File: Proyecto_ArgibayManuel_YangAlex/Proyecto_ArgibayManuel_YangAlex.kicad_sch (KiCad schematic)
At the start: 35 parts, among them J1 Conn_01x02, J10 Con_1x2, J11 Con_1x2, J2 Conn_01x01, J3 Con_1x2, J4 Con_1x2, J5 Con_1x2, J6 Con_1x2, J7 Conn_01x03, J8 Conn_01x03, J9 Conn_01x03_Pin, SW1 SW_Push, SW2 SW_Push, SW3 SW_Push, SW4 SW_Push, U1 PIC18F258-I_SO, U2 HDC2010YPAR, U3 LT1716IS5TRMPBF, U4 LT1716IS5TRMPBF, U5 TXS0108EPW, Y1 Crystal

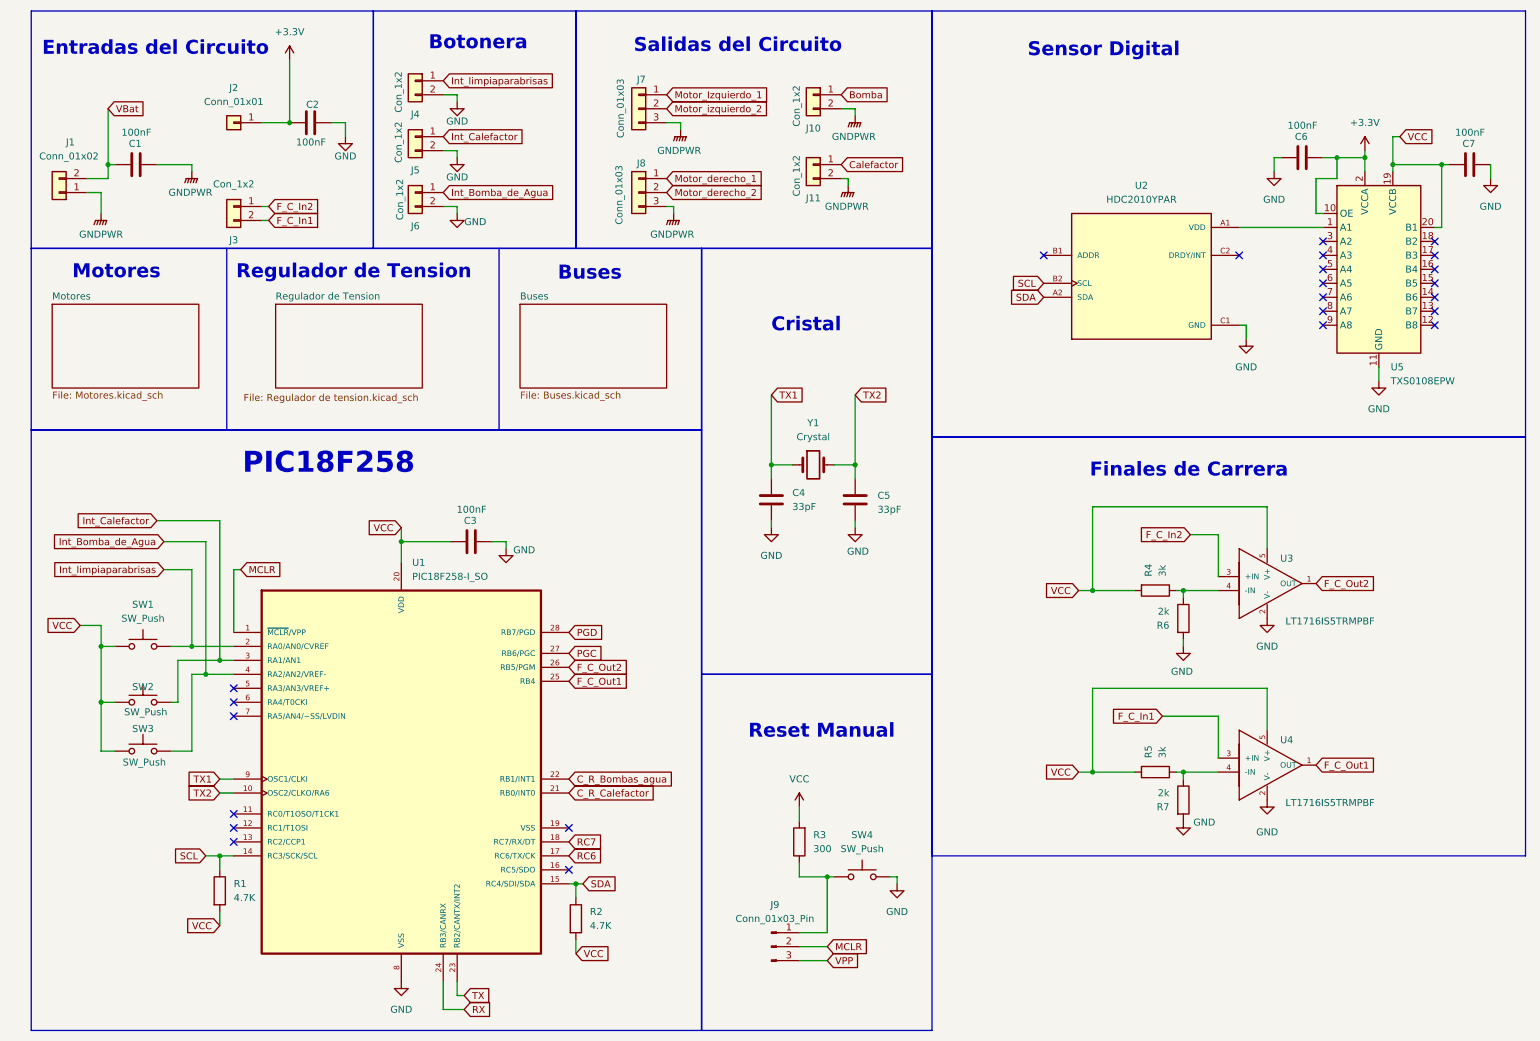
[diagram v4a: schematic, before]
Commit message: Cambio del sensor
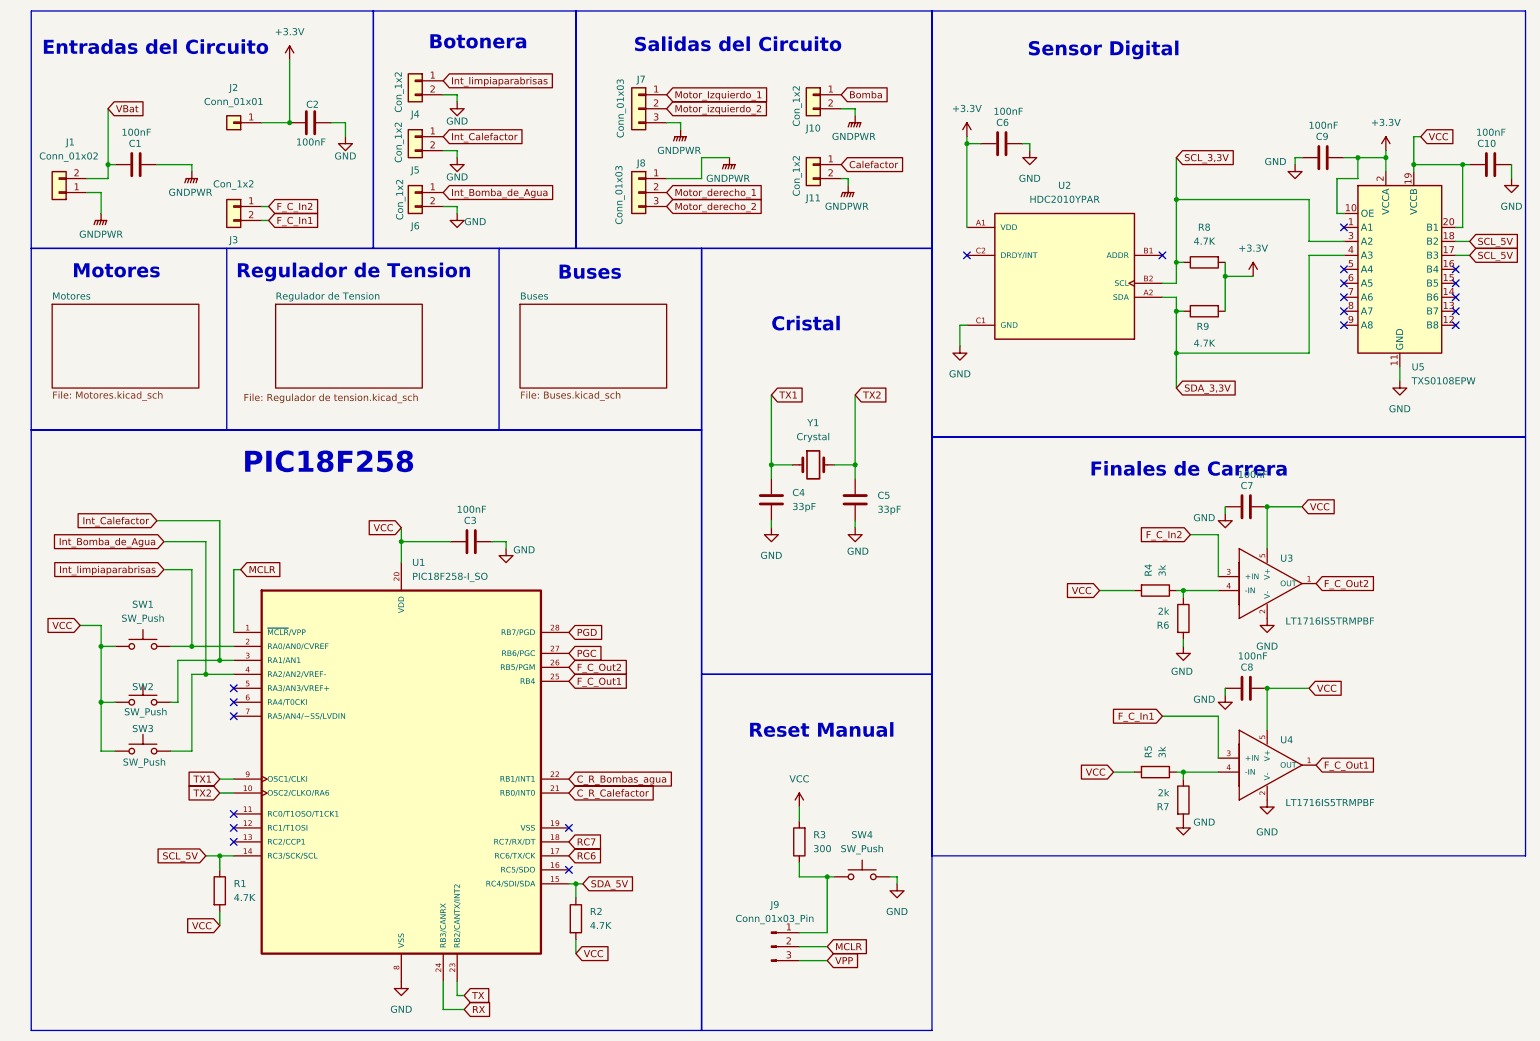
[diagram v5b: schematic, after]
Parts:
- added C6, C7, C8: 100nF, Capacitor_SMD:C_0805_2012Metric, symbol Device:C
- added R8, R9: 4.7K, Resistor_SMD:R_0805_2012Metric, symbol Device:R
- J10, J11: footprint Connector_PinHeader_2.54mm:PinHeader_1x02_P2.54mm_Vertical -> TerminalBlock_Phoenix:TerminalBlock_Phoenix_MKDS-3-2-5.08_1x02_P5.08mm_Horizontal
- J7, J8: footprint Connector_PinHeader_2.54mm:PinHeader_1x03_P2.54mm_Vertical -> TerminalBlock_Phoenix:TerminalBlock_Phoenix_MKDS-3-3-5.08_1x03_P5.08mm_Horizontal
- renumbered C7 to C10, C6 to C9
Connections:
- net +3.3V: now also U2.A1 (VDD), C6.2, R8.2, R9.2
- net GND: now also C6.1, C7.2, C8.2
- net GNDPWR: now also J8.1 (Pin_1); no longer J8.3 (Pin_3)
- net Motor_derecho_1: now also J8.2 (Pin_2); no longer J8.1 (Pin_1)
- net Motor_derecho_2: now also J8.3 (Pin_3); no longer J8.2 (Pin_2)
- net VCC: now also C7.1, C8.1
- net at U5.1 (A1): no longer U2.A1 (VDD)
- net SCL_5V: now reaches U5.17 (B3)
- net SCL_5V: now also R1.1, U1.14 (RC3/SCK/SCL), U5.18 (B2)
- net SCL_3,3V: now reaches U5.3 (A2)
- net SCL_3,3V: now also U2.B2 (SCL), R8.1
- net SDA_3,3V: now reaches U5.4 (A3)
- net SDA_3,3V: now also U2.A2 (SDA), R9.1
- removed net SCL: R1.1, U1.14 (RC3/SCK/SCL), U2.B2 (SCL)
- net SDA renamed SDA_5V
- net SDA_5V: no longer U2.A2 (SDA)
- no-connect marks 24 -> 21
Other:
- moved on the sheet: C10, C9, U2, U5

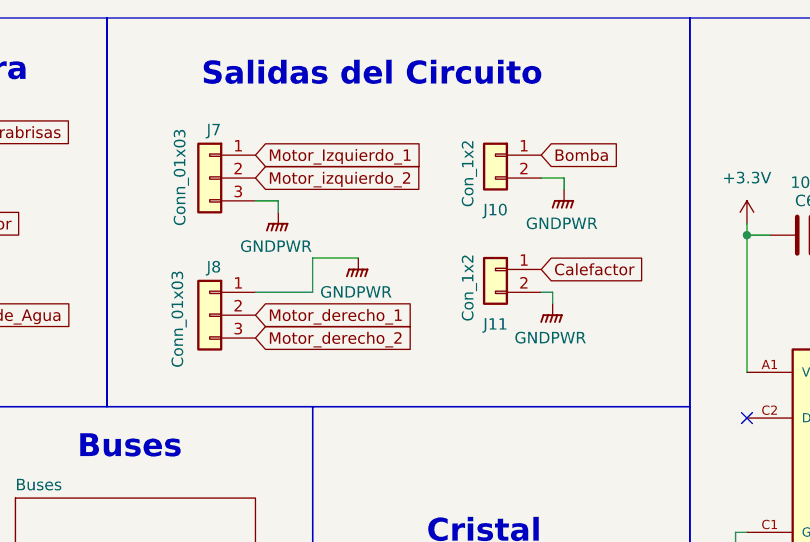
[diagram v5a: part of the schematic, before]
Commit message: Arreglo layout y esquematico (DRC correcto)
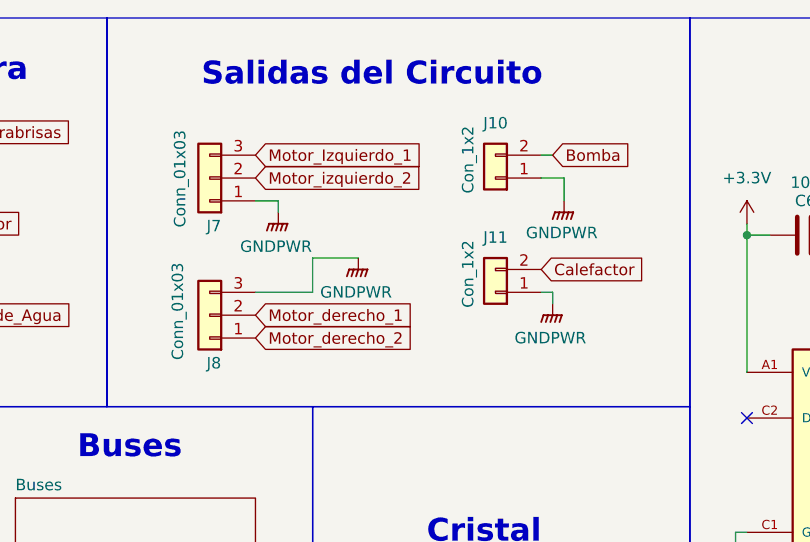
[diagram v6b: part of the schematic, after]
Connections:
- net Bomba: now also J10.2 (Pin_2); no longer J10.1 (Pin_1)
- net Calefactor: now also J11.2 (Pin_2); no longer J11.1 (Pin_1)
- net GNDPWR: now also J10.1 (Pin_1), J11.1 (Pin_1), J7.1 (Pin_1), J8.3 (Pin_3); no longer J10.2 (Pin_2), J11.2 (Pin_2), J7.3 (Pin_3), J8.1 (Pin_1)
- net Motor_Izquierdo_1: now also J7.3 (Pin_3); no longer J7.1 (Pin_1)
- net Motor_derecho_2: now also J8.1 (Pin_1); no longer J8.3 (Pin_3)
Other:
- moved on the sheet: J10, J11, J7, J8
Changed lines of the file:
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@@
 	(wire
 		(pts
+			(xy 162.56 30.48) (xy 162.56 33.02)
+		)
+		(stroke
+			(width 0)
+			(type default)
+		)
+	)
+	(wire
+		(pts
 			(xy 39.37 138.43) (xy 39.37 130.81)
 		)
@@
 	(wire
 		(pts
-			(xy 162.56 30.48) (xy 162.56 31.75)
-		)
-		(stroke
-			(width 0)
-			(type default)
-		)
-	)
-	(wire
-		(pts
 			(xy 147.32 95.25) (xy 151.13 95.25)
 		)
@@
 	(wire
 		(pts
-			(xy 245.11 74.93) (xy 245.11 57.15)
+			(xy 160.02 30.48) (xy 162.56 30.48)
 		)
 		(stroke
@@
 	(wire
 		(pts
-			(xy 25.4 45.72) (xy 25.4 49.53)
+			(xy 245.11 74.93) (xy 245.11 57.15)
 		)
 		(stroke
@@
 	(wire
 		(pts
-			(xy 49.53 114.3) (xy 49.53 125.73)
+			(xy 25.4 45.72) (xy 25.4 49.53)
 		)
 		(stroke
@@
 	(wire
 		(pts
-			(xy 160.02 30.48) (xy 162.56 30.48)
+			(xy 49.53 114.3) (xy 49.53 125.73)
 		)
 		(stroke
@@
 	(wire
 		(pts
+			(xy 160.02 27.94) (xy 161.29 27.94)
+		)
+		(stroke
+			(width 0)
+			(type default)
+		)
+	)
+	(wire
+		(pts
 			(xy 113.03 171.45) (xy 111.76 171.45)
 		)
@@
 	(global_label "Bomba"
 		(shape input)
-		(at 160.02 27.94 0)
+		(at 161.29 27.94 0)
 		(fields_autoplaced yes)
 		(effects
@@
 		)
 		(property "Intersheetrefs" "${INTERSHEET_REFS}"
-			(at 169.4155 27.94 0)
+			(at 170.6855 27.94 0)
 			(effects
 				(font
@@
 	(symbol
 		(lib_id "Connector_Generic:Conn_01x02")
-		(at 154.94 40.64 0)
-		(mirror y)
+		(at 154.94 43.18 180)
 		(unit 1)
 		(exclude_from_sim no)
@@
 		(dnp no)
 		(property "Reference" "J11"
-			(at 154.94 46.736 0)
+			(at 154.94 37.084 0)
 			(effects
 				(font
@@
 		)
 		(property "Value" "Con_1x2"
-			(at 151.892 42.672 90)
+			(at 151.892 41.148 90)
 			(effects
 				(font
@@
 		)
 		(property "Footprint" "TerminalBlock_Phoenix:TerminalBlock_Phoenix_MKDS-3-2-5.08_1x02_P5.08mm_Horizontal"
-			(at 154.94 40.64 0)
+			(at 154.94 43.18 0)
 			(effects
 				(font
@@
 		)
 		(property "Datasheet" "~"
-			(at 154.94 40.64 0)
+			(at 154.94 43.18 0)
 			(effects
 				(font
@@
 		)
 		(property "Description" "Generic connector, single row, 01x02, script generated (kicad-library-utils/schlib/autogen/connector/)"
-			(at 154.94 40.64 0)
+			(at 154.94 43.18 0)
 			(effects
 				(font
@@
 	(symbol
 		(lib_id "power:GNDPWR")
-		(at 162.56 31.75 0)
+		(at 162.56 33.02 0)
 		(unit 1)
 		(exclude_from_sim no)
@@
 		(dnp no)
 		(property "Reference" "#PWR015"
-			(at 162.56 36.83 0)
+			(at 162.56 38.1 0)
 			(effects
 				(font
@@
 		)
 		(property "Value" "GNDPWR"
-			(at 162.306 35.56 0)
+			(at 162.306 36.576 0)
 			(effects
 				(font
@@
 		)
 		(property "Footprint" ""
-			(at 162.56 33.02 0)
+			(at 162.56 34.29 0)
 			(effects
 				(font
@@
 		)
 		(property "Datasheet" ""
-			(at 162.56 33.02 0)
+			(at 162.56 34.29 0)
 			(effects
 				(font
@@
 		)
 		(property "Description" "Power symbol creates a global label with name \"GNDPWR\" , global ground"
-			(at 162.56 31.75 0)
+			(at 162.56 33.02 0)
 			(effects
 				(font
@@
 	(symbol
 		(lib_id "Connector_Generic:Conn_01x03")
-		(at 123.19 45.72 0)
-		(mirror y)
+		(at 123.19 45.72 180)
 		(unit 1)
 		(exclude_from_sim no)
@@
 		(dnp no)
 		(property "Reference" "J8"
-			(at 124.46 40.386 0)
+			(at 124.46 51.054 0)
 			(effects
 				(font
@@
 		)
 		(property "Value" "Conn_01x03"
-			(at 119.634 51.562 90)
+			(at 119.634 39.878 90)
 			(effects
 				(font
@@
 	(symbol
 		(lib_id "Connector_Generic:Conn_01x02")
-		(at 154.94 27.94 0)
-		(mirror y)
+		(at 154.94 30.48 180)
 		(unit 1)
 		(exclude_from_sim no)
@@
 		(dnp no)
 		(property "Reference" "J10"
-			(at 154.94 34.036 0)
+			(at 154.94 24.384 0)
 			(effects
 				(font
@@
 		)
 		(property "Value" "Con_1x2"
-			(at 151.892 29.972 90)
+			(at 151.892 28.448 90)
 			(effects
 				(font
@@
 		)
 		(property "Footprint" "TerminalBlock_Phoenix:TerminalBlock_Phoenix_MKDS-3-2-5.08_1x02_P5.08mm_Horizontal"
-			(at 154.94 27.94 0)
+			(at 154.94 30.48 0)
 			(effects
 				(font
@@
 		)
 		(property "Datasheet" "~"
-			(at 154.94 27.94 0)
+			(at 154.94 30.48 0)
 			(effects
 				(font
@@
 		)
 		(property "Description" "Generic connector, single row, 01x02, script generated (kicad-library-utils/schlib/autogen/connector/)"
-			(at 154.94 27.94 0)
+			(at 154.94 30.48 0)
 			(effects
 				(font
@@
 	(symbol
 		(lib_id "Connector_Generic:Conn_01x03")
-		(at 123.19 30.48 0)
-		(mirror y)
+		(at 123.19 30.48 180)
 		(unit 1)
 		(exclude_from_sim no)
@@
 		(dnp no)
 		(property "Reference" "J7"
-			(at 124.46 25.146 0)
+			(at 124.46 35.814 0)
 			(effects
 				(font
@@
 		)
 		(property "Value" "Conn_01x03"
-			(at 119.888 35.814 90)
+			(at 119.888 25.146 90)
 			(effects
 				(font

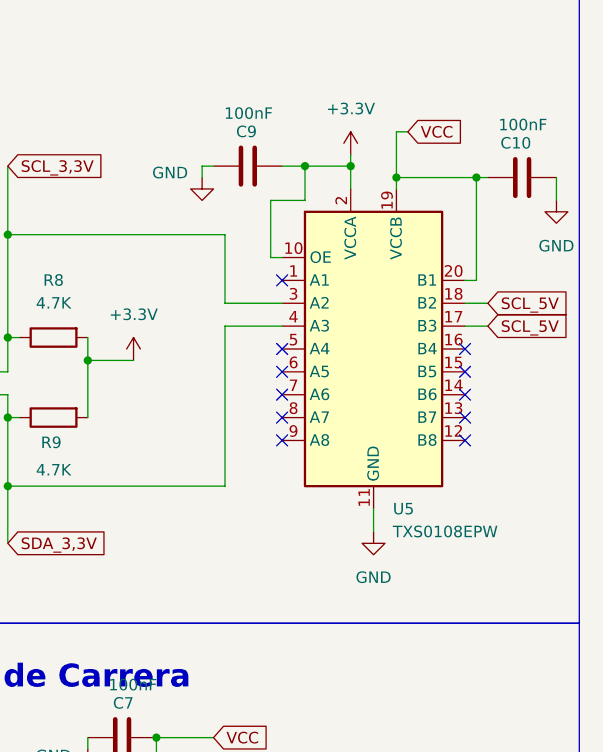
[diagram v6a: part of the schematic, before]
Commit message: Cambio de Traductor bidireccional
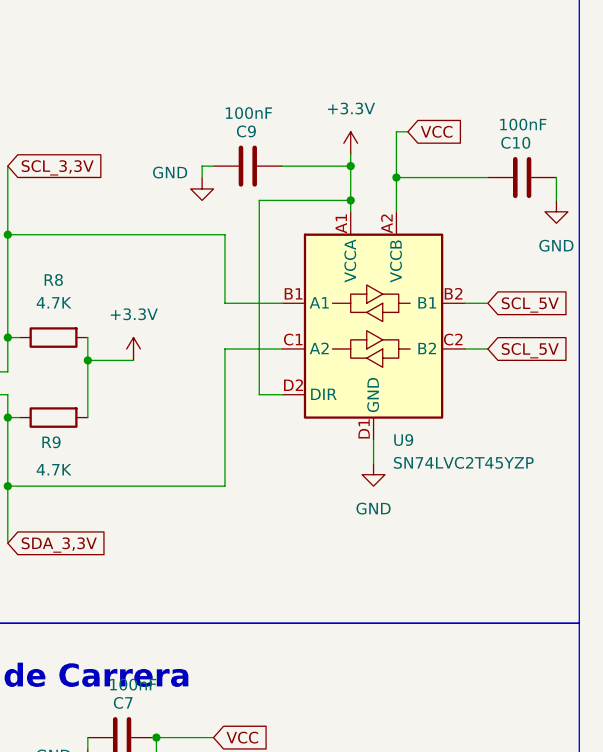
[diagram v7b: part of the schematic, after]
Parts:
- removed U5: TXS0108EPW, Package_SO:TSSOP-20_4.4x6.5mm_P0.65mm, symbol Logic_LevelTranslator:TXS0108EPW
- added U9: SN74LVC2T45YZP, Package_BGA:Texas_DSBGA-8_0.9x1.9mm_Layout2x4_P0.5mm, symbol Logic_LevelTranslator:SN74LVC2T45YZP
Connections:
- net +3.3V: now also U9.A1 (VCCA), U9.D2 (DIR)
- net GND: now also U9.D1 (GND)
- net SCL_3,3V: now also U9.B1 (A1)
- net SCL_5V: now also U9.B2 (B1), U9.C2 (B2)
- net SDA_3,3V: now also U9.C1 (A2)
- net VCC: now also U9.A2 (VCCB)
- no-connect marks 21 -> 10
